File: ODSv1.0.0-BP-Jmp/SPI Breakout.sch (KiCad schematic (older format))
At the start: 6 parts, among them J12 Conn_02x10_Odd_Even, J13 Conn_02x10_Odd_Even, J14 Conn_02x10_Odd_Even, J15 Conn_02x10_Odd_Even, J18 Conn_02x10_Odd_Even, J19 Conn_02x10_Odd_Even

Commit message: Define a no-IC variant of BP-Jmp
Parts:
- J14, J15: Config (none) -> -NoIC
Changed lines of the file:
@@
 F 7 "https://www.digikey.com/en/products/detail/samtec-inc/TSM-110-01-T-DH/2685730" H 2200 4400 50  0001 C CNN "Ordering URL"
 F 8 "SMD" H 2200 4400 50  0001 C CNN "Type"
+F 9 "-NoIC" H 2200 4400 50  0001 C CNN "Config"
 	1    2200 4400
 	1    0    0    -1
@@
 F 7 "https://www.digikey.com/en/products/detail/samtec-inc/TSM-110-01-T-DV/1236604" H 2200 5900 50  0001 C CNN "Ordering URL"
 F 8 "SMD" H 2200 5900 50  0001 C CNN "Type"
+F 9 "-NoIC" H 2200 5900 50  0001 C CNN "Config"
 	1    2200 5900
 	1    0    0    -1

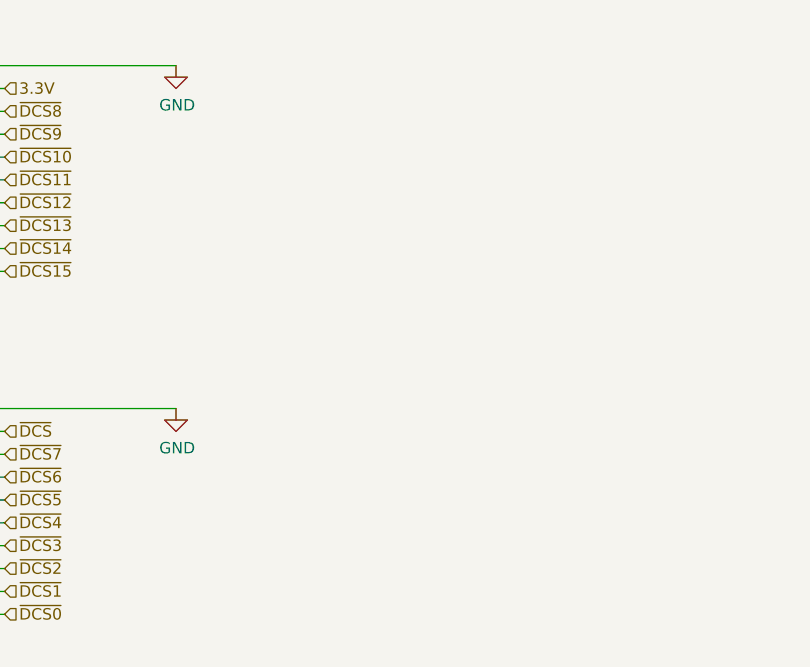
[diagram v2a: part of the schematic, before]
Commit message: Add pull-ups on demuxed DCS (#17), move pull-ups to bottom of BP-Jmp
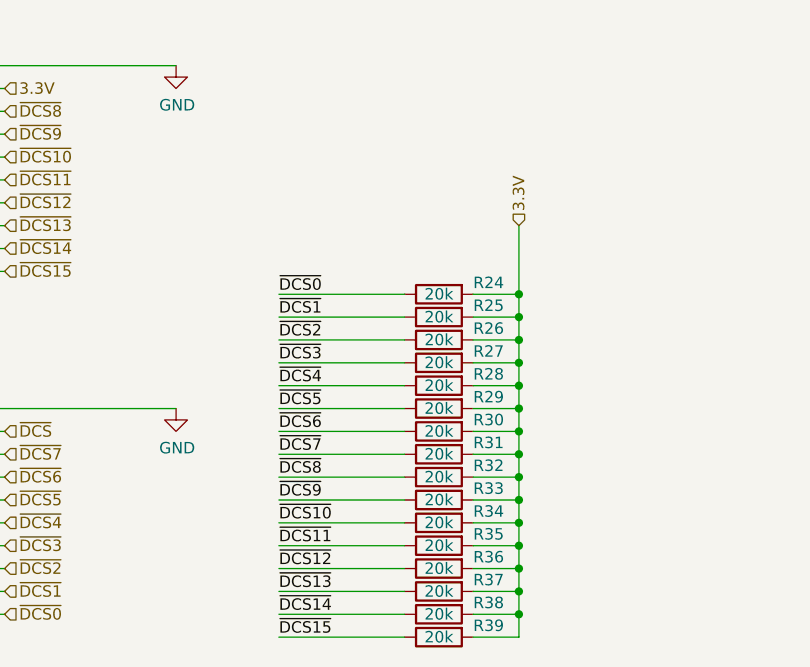
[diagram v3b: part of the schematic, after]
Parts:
- added R24, R25, R26, R27, R28, R29, R30, R31, R32, R33, R34, R35, R36, R37, R38, R39: 20k, Resistor_SMD:R_0603_1608Metric, symbol Device:R
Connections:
- net 3.3V: now also R24.2, R25.2, R26.2, R27.2, R28.2, R29.2, R30.2, R31.2, R32.2, R33.2, R34.2, R35.2, R36.2, R37.2, R38.2, R39.2
- net ~DCS0~: now also R24.1
- net ~DCS10~: now also R34.1
- net ~DCS11~: now also R35.1
- net ~DCS12~: now also R36.1
- net ~DCS13~: now also R37.1
- net ~DCS14~: now also R38.1
- net ~DCS15~: now also R39.1
- net ~DCS1~: now also R25.1
- net ~DCS2~: now also R26.1
- net ~DCS3~: now also R27.1
- net ~DCS4~: now also R28.1
- net ~DCS5~: now also R29.1
- net ~DCS6~: now also R30.1
- net ~DCS7~: now also R31.1
- net ~DCS8~: now also R32.1
- net ~DCS9~: now also R33.1

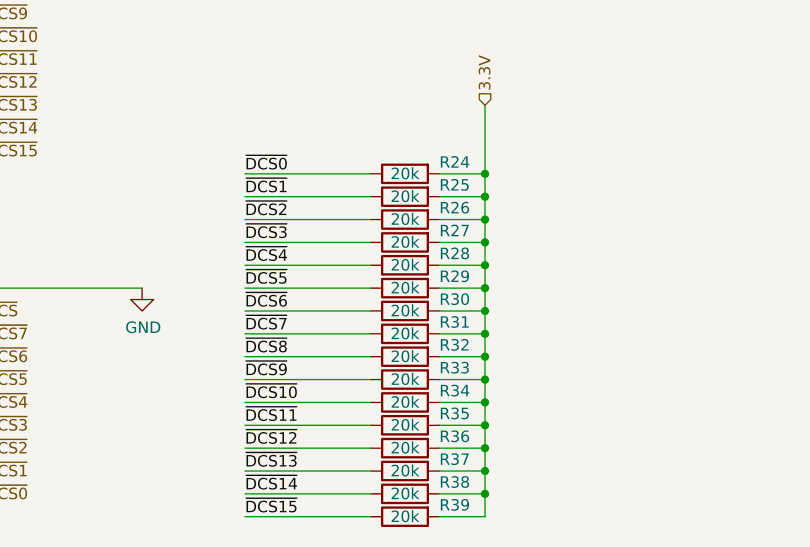
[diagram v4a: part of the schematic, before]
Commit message: Use 2k pullups instead of 20k pullups on BP-Jmp
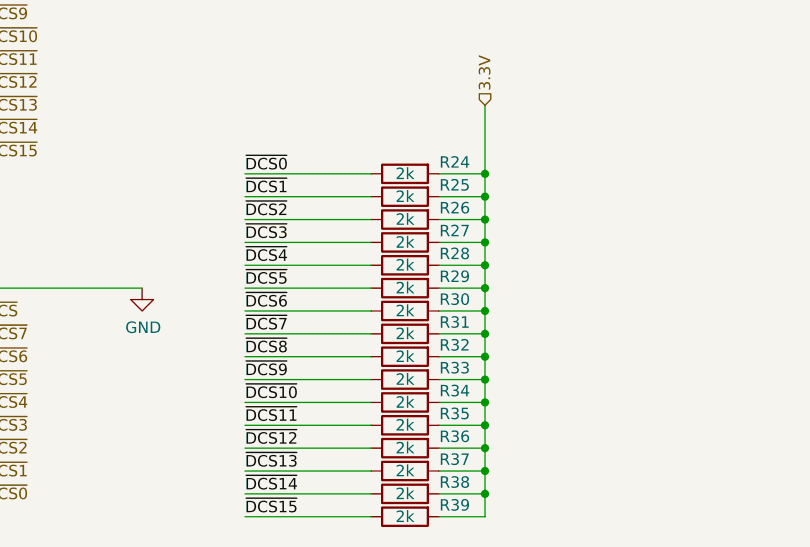
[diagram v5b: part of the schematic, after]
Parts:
- R24, R25, R26, R27, R28, R29, R30, R31, R32, R33, R34, R35, R36, R37, R38, R39: value 20k -> 2k; Digikey ID 311-20.0KHRCT-ND -> 311-2.00KHRCT-ND; MPN RC0603FR-0720KL -> RC0603FR-072KL; Ordering URL https://www.digikey.com/en/products/detail/yageo/RC0603FR-0720KL/727040 -> https://www.digikey.com/en/products/detail/yageo/RC0603FR-072KL/727009

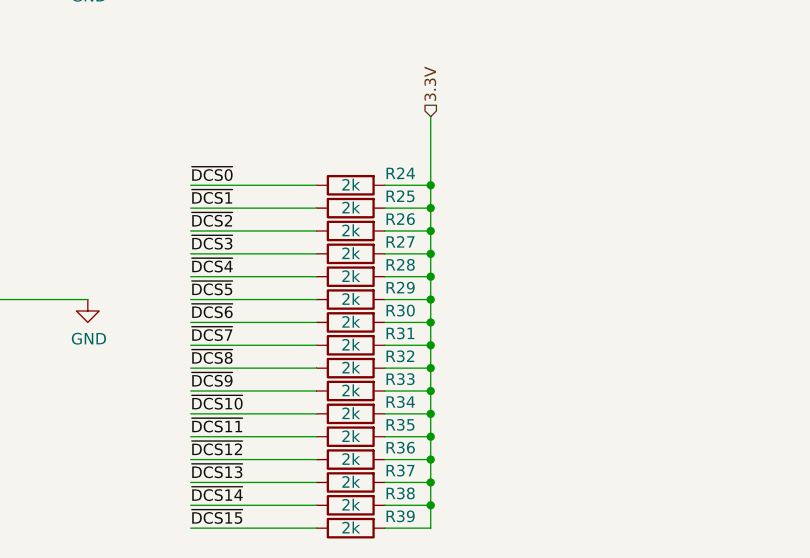
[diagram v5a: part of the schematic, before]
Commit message: Add 2k pullups within DCS selectors (#17), bump BP-Jmp to 0.2.0
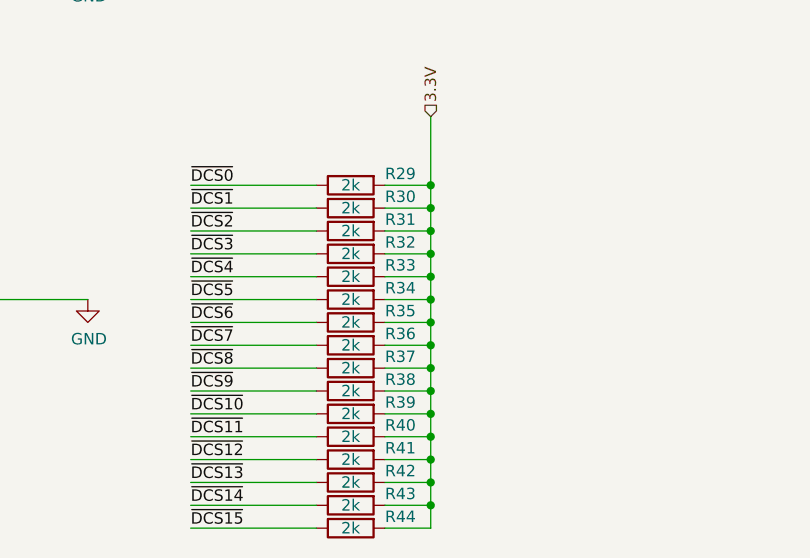
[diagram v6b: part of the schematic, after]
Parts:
- R29: renamed from R24; Config (none) -> -NoIC; Digikey ID 311-2.00KHRCT-ND -> 311-20.0KHRCT-ND; MPN RC0603FR-072KL -> RC0603FR-0720KL; Ordering URL https://www.digikey.com/en/products/detail/yageo/RC0603FR-072KL/727009 -> https://www.digikey.com/en/products/detail/yageo/RC0603FR-0720KL/727040
- R30: renamed from R25; Config (none) -> -NoIC; Digikey ID 311-2.00KHRCT-ND -> 311-20.0KHRCT-ND; MPN RC0603FR-072KL -> RC0603FR-0720KL; Ordering URL https://www.digikey.com/en/products/detail/yageo/RC0603FR-072KL/727009 -> https://www.digikey.com/en/products/detail/yageo/RC0603FR-0720KL/727040
- R31: renamed from R26; Config (none) -> -NoIC; Digikey ID 311-2.00KHRCT-ND -> 311-20.0KHRCT-ND; MPN RC0603FR-072KL -> RC0603FR-0720KL; Ordering URL https://www.digikey.com/en/products/detail/yageo/RC0603FR-072KL/727009 -> https://www.digikey.com/en/products/detail/yageo/RC0603FR-0720KL/727040
- R32: renamed from R27; Config (none) -> -NoIC; Digikey ID 311-2.00KHRCT-ND -> 311-20.0KHRCT-ND; MPN RC0603FR-072KL -> RC0603FR-0720KL; Ordering URL https://www.digikey.com/en/products/detail/yageo/RC0603FR-072KL/727009 -> https://www.digikey.com/en/products/detail/yageo/RC0603FR-0720KL/727040
- R33: renamed from R28; Config (none) -> -NoIC; Digikey ID 311-2.00KHRCT-ND -> 311-20.0KHRCT-ND; MPN RC0603FR-072KL -> RC0603FR-0720KL; Ordering URL https://www.digikey.com/en/products/detail/yageo/RC0603FR-072KL/727009 -> https://www.digikey.com/en/products/detail/yageo/RC0603FR-0720KL/727040
- R34: renamed from R29; Config (none) -> -NoIC; Digikey ID 311-2.00KHRCT-ND -> 311-20.0KHRCT-ND; MPN RC0603FR-072KL -> RC0603FR-0720KL; Ordering URL https://www.digikey.com/en/products/detail/yageo/RC0603FR-072KL/727009 -> https://www.digikey.com/en/products/detail/yageo/RC0603FR-0720KL/727040
- R35: renamed from R30; Config (none) -> -NoIC; Digikey ID 311-2.00KHRCT-ND -> 311-20.0KHRCT-ND; MPN RC0603FR-072KL -> RC0603FR-0720KL; Ordering URL https://www.digikey.com/en/products/detail/yageo/RC0603FR-072KL/727009 -> https://www.digikey.com/en/products/detail/yageo/RC0603FR-0720KL/727040
- R36: renamed from R31; Config (none) -> -NoIC; Digikey ID 311-2.00KHRCT-ND -> 311-20.0KHRCT-ND; MPN RC0603FR-072KL -> RC0603FR-0720KL; Ordering URL https://www.digikey.com/en/products/detail/yageo/RC0603FR-072KL/727009 -> https://www.digikey.com/en/products/detail/yageo/RC0603FR-0720KL/727040
- R37: renamed from R32; Config (none) -> -NoIC; Digikey ID 311-2.00KHRCT-ND -> 311-20.0KHRCT-ND; MPN RC0603FR-072KL -> RC0603FR-0720KL; Ordering URL https://www.digikey.com/en/products/detail/yageo/RC0603FR-072KL/727009 -> https://www.digikey.com/en/products/detail/yageo/RC0603FR-0720KL/727040
- R38: renamed from R33; Config (none) -> -NoIC; Digikey ID 311-2.00KHRCT-ND -> 311-20.0KHRCT-ND; MPN RC0603FR-072KL -> RC0603FR-0720KL; Ordering URL https://www.digikey.com/en/products/detail/yageo/RC0603FR-072KL/727009 -> https://www.digikey.com/en/products/detail/yageo/RC0603FR-0720KL/727040
- R39: renamed from R34; Config (none) -> -NoIC; Digikey ID 311-2.00KHRCT-ND -> 311-20.0KHRCT-ND; MPN RC0603FR-072KL -> RC0603FR-0720KL; Ordering URL https://www.digikey.com/en/products/detail/yageo/RC0603FR-072KL/727009 -> https://www.digikey.com/en/products/detail/yageo/RC0603FR-0720KL/727040
- R40: renamed from R35; Config (none) -> -NoIC; Digikey ID 311-2.00KHRCT-ND -> 311-20.0KHRCT-ND; MPN RC0603FR-072KL -> RC0603FR-0720KL; Ordering URL https://www.digikey.com/en/products/detail/yageo/RC0603FR-072KL/727009 -> https://www.digikey.com/en/products/detail/yageo/RC0603FR-0720KL/727040
- R41: renamed from R36; Config (none) -> -NoIC; Digikey ID 311-2.00KHRCT-ND -> 311-20.0KHRCT-ND; MPN RC0603FR-072KL -> RC0603FR-0720KL; Ordering URL https://www.digikey.com/en/products/detail/yageo/RC0603FR-072KL/727009 -> https://www.digikey.com/en/products/detail/yageo/RC0603FR-0720KL/727040
- R42: renamed from R37; Config (none) -> -NoIC; Digikey ID 311-2.00KHRCT-ND -> 311-20.0KHRCT-ND; MPN RC0603FR-072KL -> RC0603FR-0720KL; Ordering URL https://www.digikey.com/en/products/detail/yageo/RC0603FR-072KL/727009 -> https://www.digikey.com/en/products/detail/yageo/RC0603FR-0720KL/727040
- R43: renamed from R38; Config (none) -> -NoIC; Digikey ID 311-2.00KHRCT-ND -> 311-20.0KHRCT-ND; MPN RC0603FR-072KL -> RC0603FR-0720KL; Ordering URL https://www.digikey.com/en/products/detail/yageo/RC0603FR-072KL/727009 -> https://www.digikey.com/en/products/detail/yageo/RC0603FR-0720KL/727040
- R44: renamed from R39; Config (none) -> -NoIC; Digikey ID 311-2.00KHRCT-ND -> 311-20.0KHRCT-ND; MPN RC0603FR-072KL -> RC0603FR-0720KL; Ordering URL https://www.digikey.com/en/products/detail/yageo/RC0603FR-072KL/727009 -> https://www.digikey.com/en/products/detail/yageo/RC0603FR-0720KL/727040
